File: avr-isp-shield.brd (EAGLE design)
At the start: 68.6 x 53.3 mm, 14 parts, among them IC1 ATTINY24/44/84-PU, U2 TINY45-20-DIP, U3 ATMEGA328P_PDIP, U4 ARDUINOR3-DIMENSION

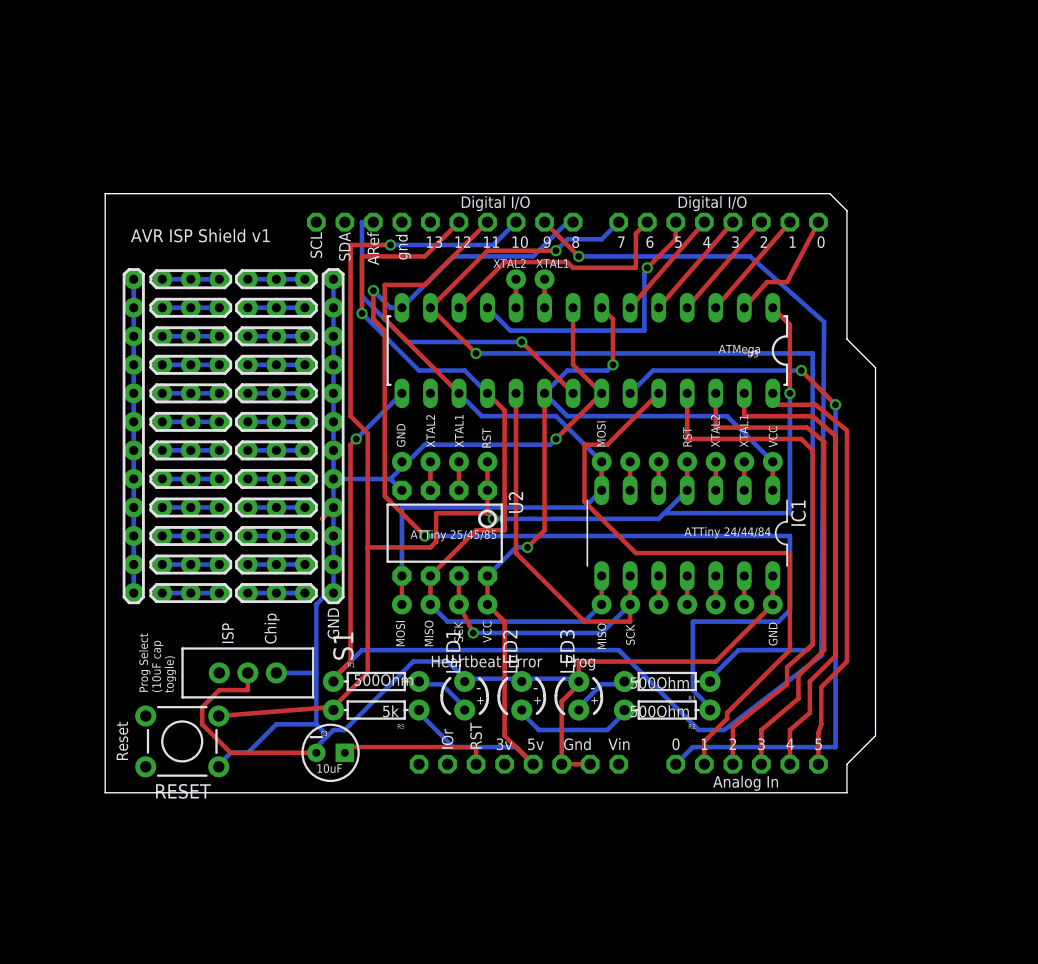
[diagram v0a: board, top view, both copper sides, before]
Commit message: added ground pours
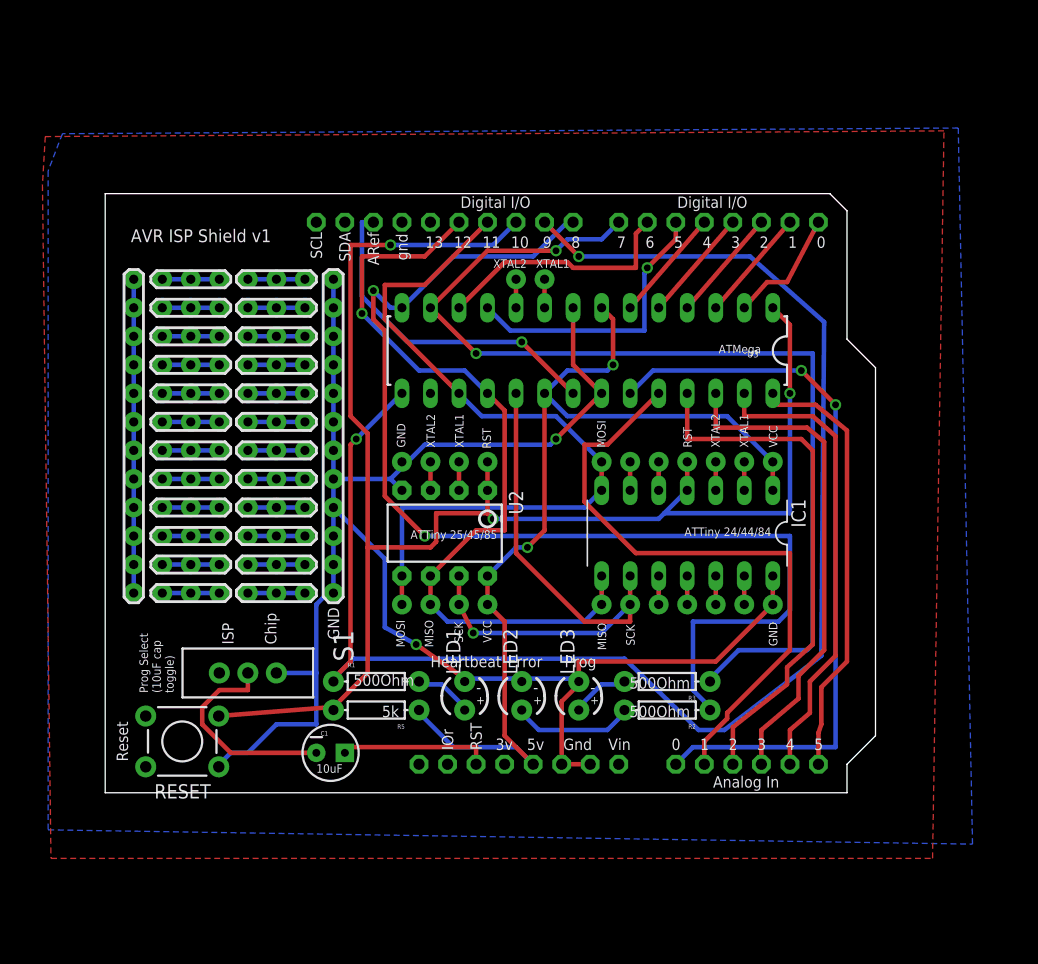
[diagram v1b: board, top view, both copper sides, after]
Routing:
- net GND: track 157.6 -> 159.0 mm, vias 15 -> 16
- net D9: track 136.2 -> 135.5 mm
- added copper zone on layer 1, net GND
- added copper zone on layer 16, net GND
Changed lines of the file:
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@@
 <param name="mtCopper" value="0.035mm 0.035mm 0.035mm 0.035mm 0.035mm 0.035mm 0.035mm 0.035mm 0.035mm 0.035mm 0.035mm 0.035mm 0.035mm 0.035mm 0.035mm 0.035mm"/>
 <param name="mtIsolate" value="1.5mm 0.15mm 0.2mm 0.15mm 0.2mm 0.15mm 0.2mm 0.15mm 0.2mm 0.15mm 0.2mm 0.15mm 0.2mm 0.15mm 0.2mm"/>
-<param name="mdWireWire" value="8mil"/>
-<param name="mdWirePad" value="8mil"/>
-<param name="mdWireVia" value="8mil"/>
-<param name="mdPadPad" value="8mil"/>
-<param name="mdPadVia" value="8mil"/>
-<param name="mdViaVia" value="8mil"/>
+<param name="mdWireWire" value="10mil"/>
+<param name="mdWirePad" value="10mil"/>
+<param name="mdWireVia" value="10mil"/>
+<param name="mdPadPad" value="10mil"/>
+<param name="mdPadVia" value="10mil"/>
+<param name="mdViaVia" value="10mil"/>
 <param name="mdSmdPad" value="8mil"/>
 <param name="mdSmdVia" value="8mil"/>
@@
 <wire x1="42.164" y1="17.78" x2="47.244" y2="17.78" width="0.4064" layer="16"/>
 <wire x1="47.244" y1="17.78" x2="47.244" y2="17.526" width="0.4064" layer="16"/>
-<wire x1="25.4" y1="13.208" x2="24.892" y2="12.7" width="0.4064" layer="16"/>
-<wire x1="24.892" y1="12.7" x2="23.876" y2="11.684" width="0.4064" layer="16"/>
-<wire x1="26.416" y1="13.208" x2="25.4" y2="13.208" width="0.4064" layer="16"/>
-<wire x1="32.512" y1="19.304" x2="26.416" y2="13.208" width="0.4064" layer="16"/>
-<wire x1="35.56" y1="19.304" x2="32.512" y2="19.304" width="0.4064" layer="16"/>
-<wire x1="37.084" y1="17.78" x2="35.56" y2="19.304" width="0.4064" layer="16"/>
 <wire x1="45.72" y1="15.748" x2="45.72" y2="10.16" width="0.4064" layer="1"/>
 <wire x1="47.244" y1="17.272" x2="45.72" y2="15.748" width="0.4064" layer="1"/>
@@
 <wire x1="30.48" y1="35.56" x2="32.004" y2="37.084" width="0.4064" layer="16"/>
 <wire x1="32.004" y1="37.084" x2="33.528" y2="38.608" width="0.4064" layer="16"/>
-<wire x1="23.876" y1="13.716" x2="24.892" y2="12.7" width="0.4064" layer="16"/>
 <wire x1="23.876" y1="24.384" x2="23.876" y2="18.288" width="0.4064" layer="16"/>
 <wire x1="23.876" y1="18.288" x2="23.876" y2="13.716" width="0.4064" layer="16"/>
@@
 <via x="25.4" y="27.94" extent="1-16" drill="0.8128" diameter="1.778"/>
 <via x="25.4" y="25.4" extent="1-16" drill="0.8128" diameter="1.778"/>
-<wire x1="25.4" y1="30.48" x2="25.4" y2="53.34" width="0.4064" layer="16"/>
+<wire x1="25.4" y1="30.48" x2="25.4" y2="33.02" width="0.4064" layer="16"/>
 <via x="31.496" y="37.084" extent="1-16" drill="0.8128" diameter="1.778" shape="octagon"/>
+<wire x1="25.4" y1="33.02" x2="25.4" y2="53.34" width="0.4064" layer="16"/>
 <wire x1="24.892" y1="25.4" x2="25.4" y2="25.4" width="0.4064" layer="16"/>
 <wire x1="31.496" y1="37.084" x2="32.004" y2="37.084" width="0.4064" layer="16"/>
 <contactref element="S1" pad="1"/>
-<wire x1="24.384" y1="32.004" x2="25.4" y2="33.02" width="0.4064" layer="1"/>
 <wire x1="20.32" y1="13.716" x2="17.78" y2="11.176" width="0.4064" layer="16"/>
 <wire x1="23.876" y1="13.716" x2="20.32" y2="13.716" width="0.4064" layer="16"/>
 <wire x1="20.32" y1="18.288" x2="23.876" y2="18.288" width="0.4064" layer="16"/>
-<wire x1="25.4" y1="48.26" x2="25.4" y2="50.8" width="0" layer="19" extent="1-1"/>
-<wire x1="25.4" y1="45.72" x2="25.4" y2="48.26" width="0" layer="19" extent="1-1"/>
-<wire x1="25.4" y1="43.18" x2="25.4" y2="45.72" width="0" layer="19" extent="1-1"/>
-<wire x1="25.4" y1="40.64" x2="25.4" y2="43.18" width="0" layer="19" extent="1-1"/>
-<wire x1="25.4" y1="38.1" x2="25.4" y2="40.64" width="0" layer="19" extent="1-1"/>
-<wire x1="25.4" y1="35.56" x2="25.4" y2="38.1" width="0" layer="19" extent="1-1"/>
-<wire x1="25.4" y1="33.02" x2="25.4" y2="35.56" width="0" layer="19" extent="1-1"/>
-<wire x1="25.4" y1="30.48" x2="24.384" y2="32.004" width="0" layer="19" extent="1-1"/>
-<wire x1="25.4" y1="27.94" x2="25.4" y2="25.908" width="0" layer="19" extent="16-16"/>
+<wire x1="29.972" y1="28.448" x2="25.4" y2="33.02" width="0.4064" layer="16"/>
+<wire x1="29.972" y1="22.352" x2="29.972" y2="28.448" width="0.4064" layer="16"/>
+<wire x1="32.766" y1="20.828" x2="29.972" y2="22.352" width="0.4064" layer="16"/>
+<wire x1="37.084" y1="17.78" x2="32.766" y2="20.828" width="0.4064" layer="1"/>
+<wire x1="37.084" y1="17.78" x2="37.084" y2="17.526" width="0.4064" layer="1"/>
+<via x="32.766" y="20.828" extent="1-16" drill="0.6096"/>
+<polygon width="0.4064" layer="1">
+<vertex x="-0.508" y="61.722"/>
+<vertex x="0.254" y="1.778"/>
+<vertex x="78.74" y="1.778"/>
+<vertex x="79.756" y="66.548"/>
+<vertex x="-0.254" y="66.04"/>
+</polygon>
+<polygon width="0.4064" layer="16">
+<vertex x="0" y="62.992"/>
+<vertex x="0" y="4.318"/>
+<vertex x="82.296" y="3.048"/>
+<vertex x="81.026" y="66.802"/>
+<vertex x="1.27" y="66.294"/>
+</polygon>
 </signal>
 <signal name="VCC">
@@
 <wire x1="47.244" y1="55.372" x2="44.196" y2="58.42" width="0.4064" layer="1"/>
 <wire x1="62.484" y1="55.372" x2="47.244" y2="55.372" width="0.4064" layer="16"/>
-<wire x1="50.8" y1="20.32" x2="57.912" y2="13.208" width="0.4064" layer="16"/>
-<wire x1="27.94" y1="20.32" x2="50.8" y2="20.32" width="0.4064" layer="16"/>
-<wire x1="25.4" y1="17.78" x2="27.94" y2="20.32" width="0.4064" layer="16"/>
+<wire x1="51.308" y1="19.558" x2="57.912" y2="13.208" width="0.4064" layer="16"/>
+<wire x1="27.178" y1="19.558" x2="51.308" y2="19.558" width="0.4064" layer="16"/>
+<wire x1="25.4" y1="17.78" x2="27.178" y2="19.558" width="0.4064" layer="16"/>
 <wire x1="25.4" y1="17.78" x2="25.4" y2="17.526" width="0.4064" layer="16"/>
 <via x="47.244" y="55.372" extent="1-16" drill="0.6096"/>

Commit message: routing SCK correctly
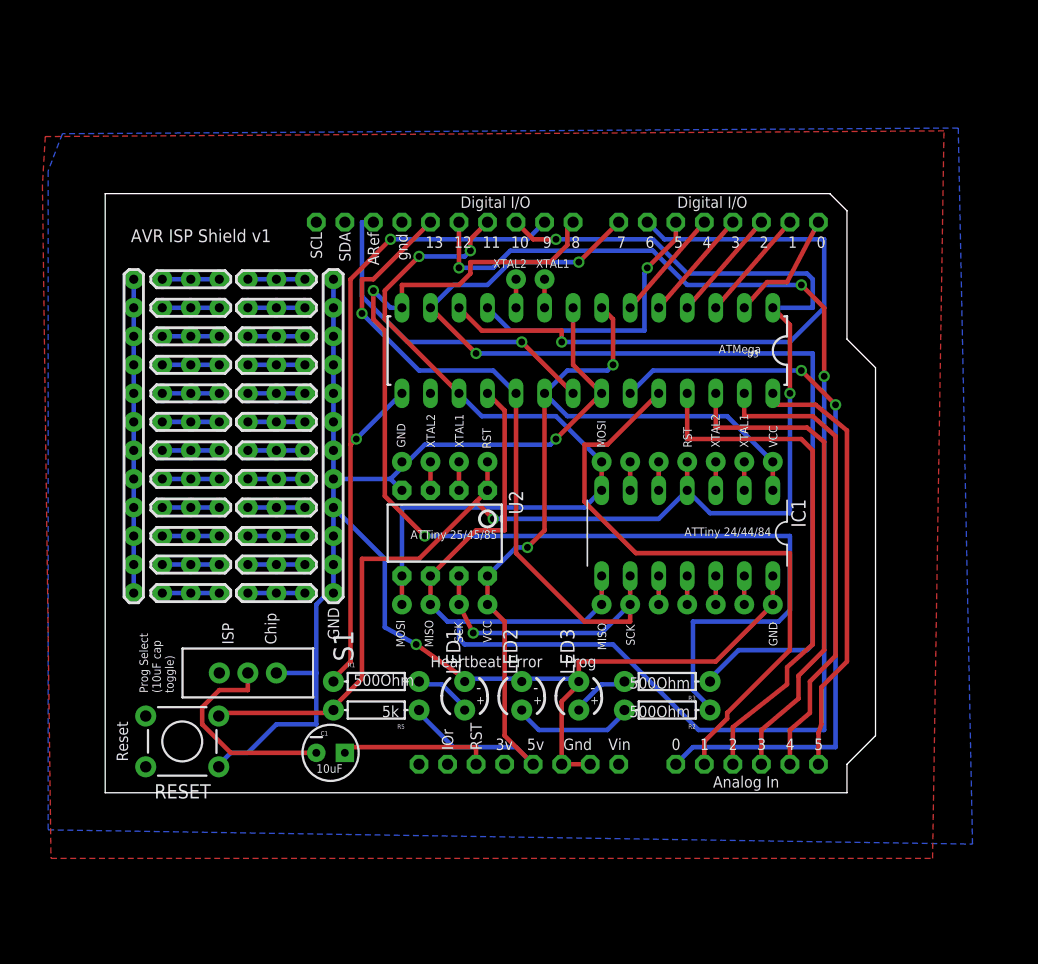
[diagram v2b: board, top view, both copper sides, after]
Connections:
- net SCK: now also U4.D13
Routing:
- net MISO: track 71.8 -> 157.0 mm, vias 3 -> 5
- net D9: track 135.5 -> 62.3 mm
- net D6: track 22.1 -> 58.1 mm, vias 0 -> 1
- net SCK: track 51.4 -> 79.3 mm, vias 3 -> 4
- net RST: track 138.8 -> 128.0 mm
- net D8: track 102.0 -> 104.7 mm
- net MOSI: track 68.7 -> 69.0 mm, vias 2 -> 4

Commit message: v1
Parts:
- R1, R2, R3: value 500Ohm -> 500
- moved R2 6.86 mm to (62.0, 14.7)
- moved R3 6.86 mm to (62.0, 17.3)
- moved LED3 5.33 mm to (52.6, 16.3)
- moved LED2 3.05 mm to (45.2, 16.3)
- moved LED1 1.27 mm to (38.4, 16.3)
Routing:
- net GND: track 159.0 -> 113.5 mm, vias 16 -> 14
- net D8: track 104.7 -> 99.7 mm
- net D7: track 92.2 -> 87.8 mm
- net MISO: track 157.0 -> 161.1 mm, vias 5 -> 2
- net A2: track 47.0 -> 50.7 mm
- net N$6: track 10.9 -> 14.5 mm
- net A3: track 44.3 -> 47.4 mm
- net A4: track 41.8 -> 44.1 mm
- net N$7: track 5.41 -> 6.53 mm
- net N$5: track 5.41 -> 6.45 mm
- net VCC: track 87.7 -> 88.6 mm
- net A5: track 39.1 -> 40.0 mm
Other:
- board text added: "(10uF switch)"
- board text added: "Prog Select"
- board text removed: "Prog Select (10uF cap toggle)"
